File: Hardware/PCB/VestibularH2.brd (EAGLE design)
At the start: 58 x 52.5 mm, 79 parts, among them IC1 FT232RL, IC10 THS4281DBVT, IC11 M74VHC1GT126DT1G, IC12 M74VHC1GT126DT1G, IC2 M74VHC1GT126DT1G, IC3 LP5907MFX-3.3, IC4 M74VHC1GT126DT1G, IC5 M74VHC1GT126DT1G, IC6 M74VHC1GT126DT1G, IC7 USBLC6-2SC6, IC8 ATXMEGA32A4U, IC9 LP5907MFX-3.3, X1 1x5 MAIN PLUG, X2 1x5 case, X3 1x2 case, X4 1x3 case, X5 1x5 case, X6 USB_MINI_B, X7 DC_JACK2.1MM, X8 CLCK_JACK

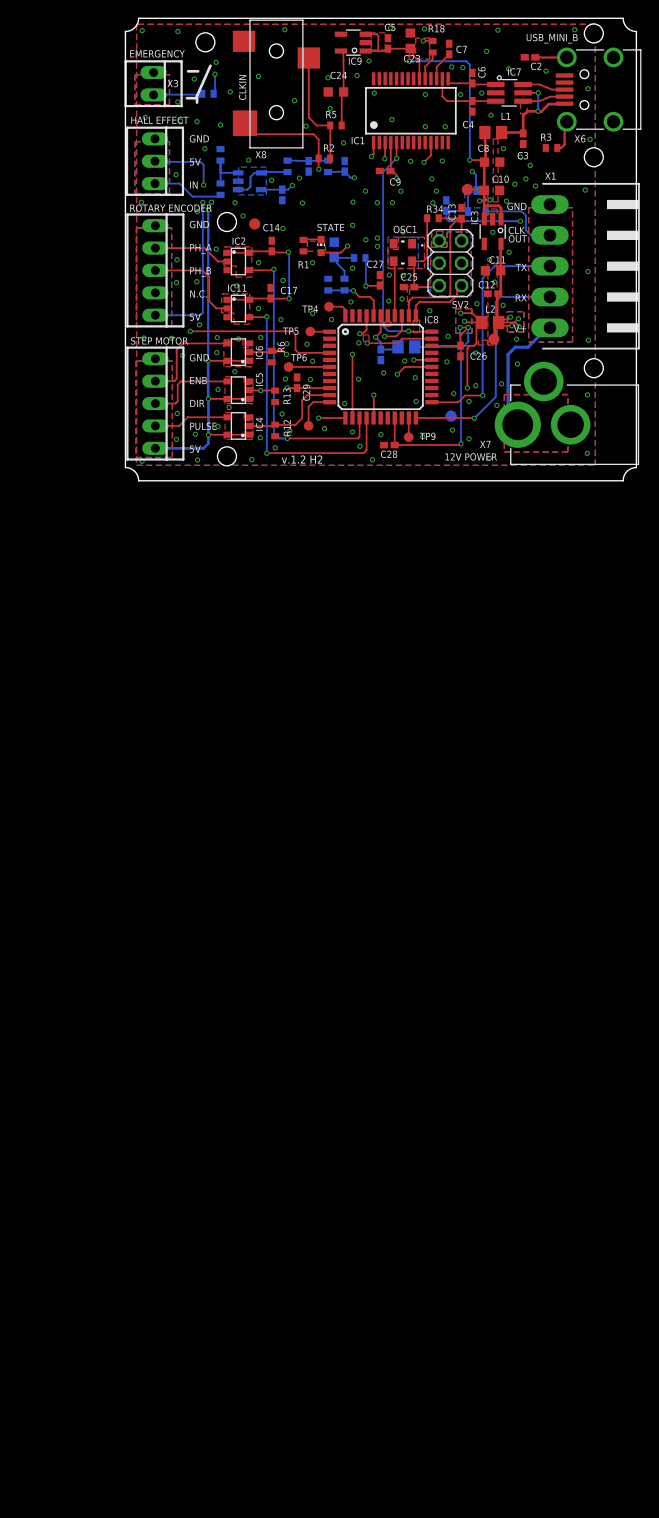
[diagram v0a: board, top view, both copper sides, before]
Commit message: Created the schematic with new ios.
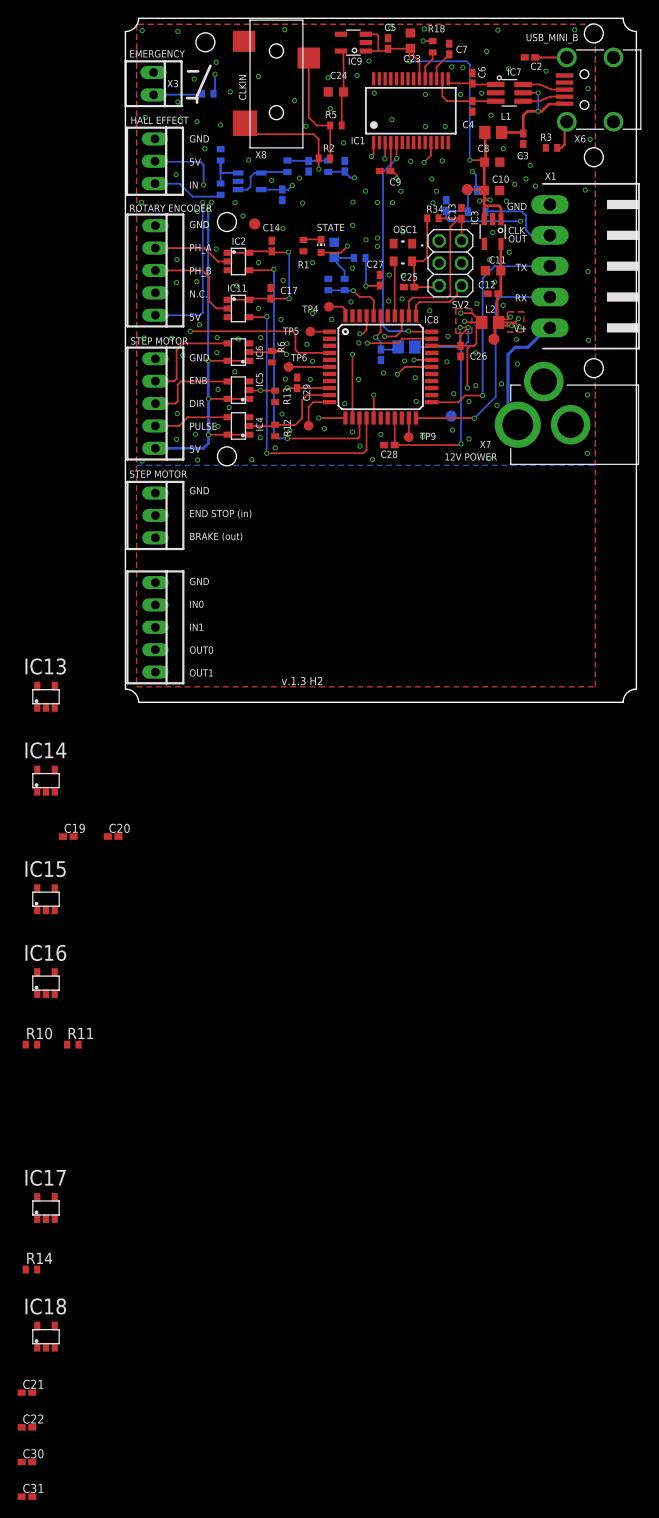
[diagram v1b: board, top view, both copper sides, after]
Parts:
- added C19, C20, C21, C22, C30, C31: 100nF, Harp Motor H2-module v1.0:C0402K
- added IC13, IC14, IC15, IC16, IC17, IC18: M74VHC1GT126DT1G, Harp Motor H2-module v1.0:TSOP-5
- added R10, R11, R14: 10k, Harp Motor H2-module v1.0:R0402
- added X10: 1x3 case, Harp Motor H2-module v1.0:22-23-2031
- added X9: 1x5 case, Harp Motor H2-module v1.0:22-23-2051
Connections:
- net ENCODER_A_PHASE renamed INPUT1
- net ENCODER_B_PHASE renamed INPUT0
- net U_ENCODER_A_PHASE renamed U_PH_B
- net U_ENCODER_B_PHASE renamed U_PH_A
- new net BRAKE: IC17.4, X10.3
- new net ENDSTOP: IC18.2, X10.2
- new net IN0: IC13.2, X9.2
- new net IN1: IC14.2, X9.3
- new net OUTPUT0: IC16.4, X9.4
- new net OUTPUT1: IC15.4, X9.5
- new net UC_BRAKE: IC17.2, R14.2
- new net UC_ENDSTOP: IC18.4, IC8.17
- new net UC_INPUT0: IC13.4, IC8.25
- new net UC_INPUT1: IC14.4, IC8.26
- new net UC_OUTPUT0: IC16.2, R10.2
- new net UC_OUTPUT1: IC15.2, R11.2
- net +3V3: now also C19.1, C20.1, C21.1, IC13.1, IC13.5, IC14.1, IC14.5, IC18.1, IC18.5
- net +5V: now also C22.1, C30.1, C31.1, IC15.1, IC15.5, IC16.1, IC16.5, IC17.1, IC17.5
- net GND: now also C19.2, C20.2, C21.2, C22.2, C30.2, C31.2, IC13.3, IC14.3, IC15.3, IC16.3, IC17.3, IC18.3, R10.1, R11.1, R14.1, X10.1, X9.1
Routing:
- removed copper zone on layer 15, net N$10
- removed copper zone on layer 2, net N$14
- removed copper zone on layer 1, net N$16
- removed copper zone on layer 16, net N$19
- removed copper zone on layer 15, net N$20
- removed copper zone on layer 2, net N$21
- removed copper zone on layer 1, net N$22
- removed copper zone on layer 16, net N$23
- removed copper zone on layer 15, net N$24
- removed copper zone on layer 2, net N$25
- removed copper zone on layer 1, net N$26
- removed copper zone on layer 16, net N$27
- removed copper zone on layer 15, net N$28
- removed copper zone on layer 2, net N$29
- removed copper zone on layer 1, net N$30
- removed copper zone on layer 16, net N$31
- removed copper zone on layer 15, net N$32
- removed copper zone on layer 2, net N$33
- removed copper zone on layer 1, net N$34
- removed copper zone on layer 16, net N$35
- removed copper zone on layer 15, net N$36
- removed copper zone on layer 2, net N$37
- removed copper zone on layer 1, net N$39
- removed copper zone on layer 16, net N$4
- removed copper zone on layer 16, net N$40
- removed copper zone on layer 2, net N$41
- removed copper zone on layer 1, net N$42
- removed copper zone on layer 15, net N$43
- removed copper zone on layer 16, net N$44
- removed copper zone on layer 1, net N$45
- removed copper zone on layer 1, net N$46
- removed copper zone on layer 1, net N$47
- removed copper zone on layer 1, net N$48
- removed copper zone on layer 1, net N$49
- removed copper zone on layer 15, net N$5
- removed copper zone on layer 1, net N$52
- removed copper zone on layer 1, net N$53
- removed copper zone on layer 1, net N$54
- removed copper zone on layer 1, net N$55
- removed copper zone on layer 1, net N$56
- removed copper zone on layer 1, net N$57
- removed copper zone on layer 1, net N$58
- removed copper zone on layer 2, net N$6
- removed copper zone on layer 1, net N$60
- removed copper zone on layer 16, net N$66
- removed copper zone on layer 1, net N$7
- removed copper zone on layer 16, net N$8
- removed copper zone on layer 1, net X1
- removed copper zone on layer 1, net X2
- removed copper zone on layer 1, net X3
- removed copper zone on layer 1, net X4
- removed copper zone on layer 1, net X5
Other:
- board size 58 x 52.5 mm -> 58 x 77.6 mm
- board text added: "GND END STOP (in) BRAKE (out)"
- board text added: "GND IN0 IN1 OUT0 OUT1"
- board text added: "v.1.3 H2"
- board text removed: "v.1.2 H2"

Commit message: Finalized the layout.
Co-Authored-By: David Palma <78764277+davidpalma666@users.noreply.github.com>
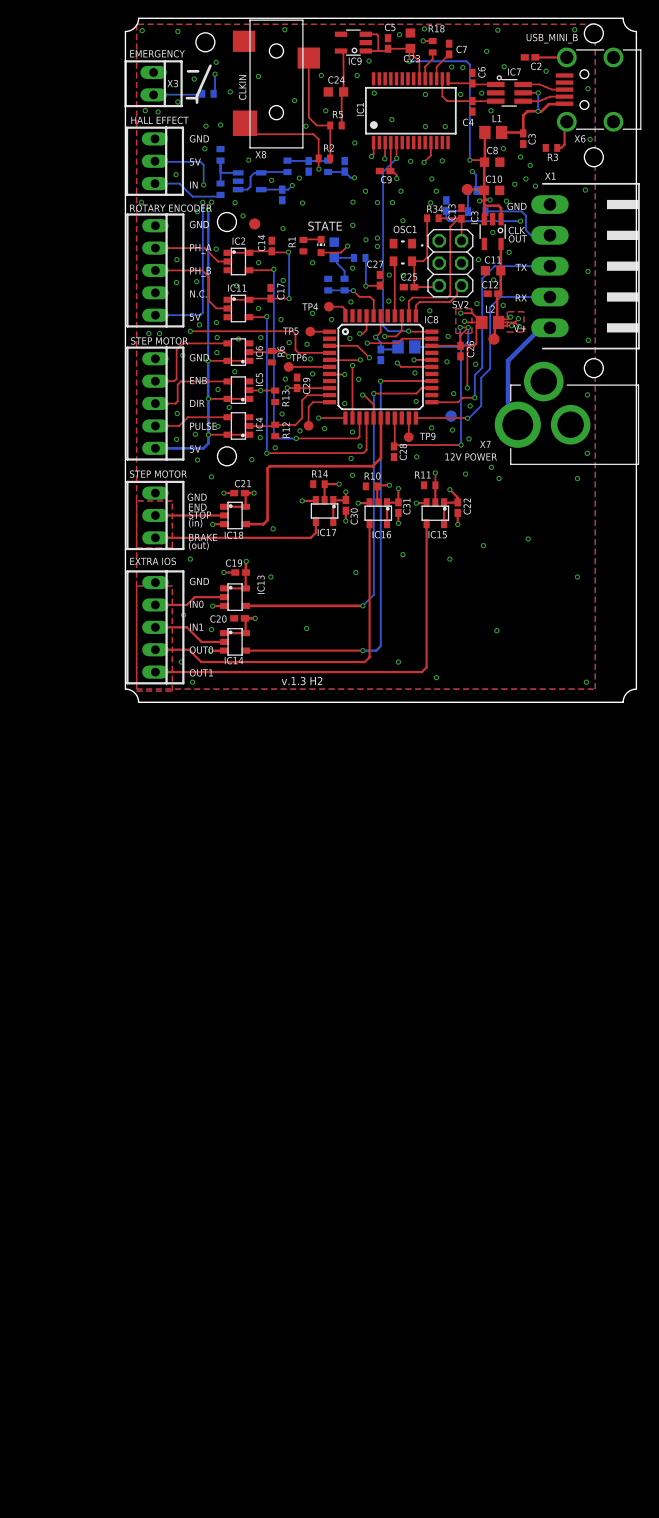
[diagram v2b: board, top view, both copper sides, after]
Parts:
- moved C31 119.9 mm to (31.0, -3.05), turned to 270 degrees
- moved C22 115.3 mm to (37.7, -3.05), turned to 270 degrees
- moved C30 114.5 mm to (25.0, -2.79), turned to 270 degrees
- moved C21 104.9 mm to (13.0, -1.40), turned to 180 degrees
- moved IC18 95.7 mm to (12.4, -3.94), turned to 270 degrees
- moved R14 94.9 mm to (22.0, -0.38)
- moved IC17 85.2 mm to (22.6, -3.43), turned to 180 degrees
- moved R11 75.3 mm to (34.5, -0.51)
- moved R10 74.2 mm to (27.9, -0.64)
- moved IC16 65.3 mm to (28.7, -3.68), turned to 180 degrees
- moved IC15 62.2 mm to (35.2, -3.68), turned to 180 degrees
- moved C19 35.8 mm to (13.1, -10.4), turned to 180 degrees
- moved C20 28.6 mm to (13.0, -15.6), turned to 180 degrees
- moved IC14 26.6 mm to (12.4, -18.3), turned to 270 degrees
- moved IC13 24.3 mm to (12.4, -13.2), turned to 270 degrees
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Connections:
- net UC_BRAKE: now also IC8.7
- net UC_OUTPUT0: now also IC8.5
- net UC_OUTPUT1: now also IC8.3
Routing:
- net +3V3: track 202.3 -> 287.3 mm, vias 15 -> 19
- net +5V: track 188.7 -> 257.3 mm, vias 10 -> 13
- net UC_INPUT1: track 0.00 -> 51.5 mm, vias 0 -> 2
- net OUTPUT1: track 0.00 -> 47.3 mm
- net UC_INPUT0: track 0.00 -> 44.8 mm, vias 0 -> 2
- net OUTPUT0: track 0.00 -> 40.3 mm
- net UC_OUTPUT1: track 0.00 -> 28.4 mm, vias 0 -> 2
- net UC_ENDSTOP: track 0.00 -> 26.5 mm
- net UC_OUTPUT0: track 0.00 -> 23.7 mm, vias 0 -> 2
- net BRAKE: track 0.00 -> 19.7 mm
- net UC_BRAKE: track 0.00 -> 17.9 mm, vias 0 -> 2
- net GND: track 0.00 -> 14.5 mm, vias 147 -> 172
- net IN1: track 0.00 -> 8.53 mm
- net IN0: track 0.00 -> 8.21 mm
- net ENDSTOP: track 0.00 -> 7.85 mm
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- added copper zone on layer 15, net N$51
- added copper zone on layer 16, net N$59
- added copper zone on layer 1, net N$61
- added copper zone on layer 2, net N$67
- added copper zone on layer 1, net N$68
- added copper zone on layer 2, net N$69
- added copper zone on layer 15, net N$70
- added copper zone on layer 16, net N$71
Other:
- board text added: "BRAKE (out)"
- board text added: "END STOP (in)"
- board text added: "EXTRA IOS"
- board text added: "GND"
- board text removed: "GND END STOP (in) BRAKE (out)"
